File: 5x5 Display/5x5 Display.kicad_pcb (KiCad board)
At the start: 2 copper layers, 129.5 x 129.5 mm, 29 parts, among them J1 TOP, J2 RIGHT, J3 BOTTOM, J4 LEFT

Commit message: buck layout
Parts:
- removed J1: TOP, Magnetic pogo pins:Magnetic Pogo Pin connector 4P
- removed J2: RIGHT, Magnetic pogo pins:Magnetic Pogo Pin connector 4P
- removed J3: BOTTOM, Magnetic pogo pins:Magnetic Pogo Pin connector 4P
- removed J4: LEFT, Magnetic pogo pins:Magnetic Pogo Pin connector 4P
- added C1: 47nF, Capacitor_SMD:C_0603_1608Metric, B.Cu at (19.7, 170.6)
- added C2: 30μF, Capacitor_SMD:C_1206_3216Metric, F.Cu at (236.0, 97.5)
- added C3: 0.1μF, Capacitor_SMD:C_0603_1608Metric, F.Cu at (240.3, 93.7)
- added C4: 30μF, Capacitor_SMD:C_1206_3216Metric, F.Cu at (250.4, 98.7)
- added C5: 30μF, Capacitor_SMD:C_1206_3216Metric, F.Cu at (214.4, 97.5)
- added C6: 0.1μF, Capacitor_SMD:C_0603_1608Metric, F.Cu at (218.8, 93.7)
- added C7: 30μF, Capacitor_SMD:C_1206_3216Metric, F.Cu at (228.9, 98.7)
- added C8: 0.1μF, Capacitor_SMD:C_0603_1608Metric, B.Cu at (28.3, 92.0)
- added C9: 0.33μF, Capacitor_SMD:C_0603_1608Metric, B.Cu at (28.3, 89.0)
- added D1: POWER, LED_SMD:LED_0805_2012Metric, B.Cu at (19.8, 100.2)
- added D10: ≥5V, Diode_SMD:D_SOD-323, F.Cu at (1.67, 0.97)
- added D2: FUSE FAULT, LED_SMD:LED_0805_2012Metric, B.Cu at (19.8, 97.1)
- added D3: 3.3V FAULT, LED_SMD:LED_0805_2012Metric, B.Cu at (19.8, 94.1)
- added D4: 5V FAULT, LED_SMD:LED_0805_2012Metric, B.Cu at (19.8, 91.0)
- added D5: CLOCK, LED_SMD:LED_0805_2012Metric, B.Cu at (19.8, 88.0)
- added D6: ≥33V, Diode_SMD:D_SMA, B.Cu at (10.9, 51.1)
- added D7: ≥33V, Diode_SMD:D_SMA, B.Cu at (10.9, 46.6)
- added D8: ≥33V, Diode_SMD:D_SMA, B.Cu at (10.9, 42.0)
- added D9: ≥33V, Diode_SMD:D_SMA, B.Cu at (10.9, 37.5)
- added FUSE1: TPS1663x (VQFN), Package_DFN_QFN:VQFN-24-1EP_4x4mm_P0.5mm_EP2.5x2.5mm_ThermalVias, B.Cu at (20.6, 175.3)
- added L1: 2.2μH, Inductor_SMD:L_6.3x6.3_H3, F.Cu at (245.4, 97.2)
- added L2: 3.3μH, Inductor_SMD:L_6.3x6.3_H3, F.Cu at (223.8, 97.2)
- added NT1: NT, NetTie:NetTie-2_SMD_Pad0.5mm, F.Cu at (0.75, 0.25)
- added NT1: NT, NetTie:NetTie-2_SMD_Pad0.5mm, F.Cu at (239.6, 98.3)
- added NT2: NT, NetTie:NetTie-2_SMD_Pad0.5mm, F.Cu at (218.1, 98.3)
- added POGO1: Left - Pins, Connector_PinSocket_2.54mm:PinSocket_1x05_P2.54mm_Horizontal, F.Cu at (73.7, 80.0)
- added POGO2: Top - Pins, Connector_PinSocket_2.54mm:PinSocket_1x05_P2.54mm_Horizontal, F.Cu at (141.0, 22.9)
- added POGO3: Right - Socket, Connector_PinSocket_2.54mm:PinSocket_1x05_P2.54mm_Horizontal, F.Cu at (198.1, 90.2)
- added POGO4: Bottom - Socket, Connector_PinSocket_2.54mm:PinSocket_1x05_P2.54mm_Horizontal, F.Cu at (130.8, 147.3)
- added R1: 1.5MΩ, Resistor_SMD:R_0603_1608Metric, B.Cu at (15.5, 177.2)
- added R10: 1kΩ, Resistor_SMD:R_0603_1608Metric, B.Cu at (24.0, 100.4)
- added R11: 1.5kΩ, Resistor_SMD:R_0603_1608Metric, B.Cu at (24.0, 97.9)
- added R12: 1.5kΩ, Resistor_SMD:R_0603_1608Metric, B.Cu at (24.0, 95.4)
- added R13: 1.5kΩ, Resistor_SMD:R_0603_1608Metric, B.Cu at (24.0, 92.9)
- added R14: 1.5kΩ, Resistor_SMD:R_0603_1608Metric, B.Cu at (24.0, 90.4)
- added R2: 430kΩ, Resistor_SMD:R_0603_1608Metric, B.Cu at (15.5, 174.7)
- added R3: 75kΩ, Resistor_SMD:R_0603_1608Metric, B.Cu at (15.5, 172.1)
- added R4: 5.6kΩ, Resistor_SMD:R_0603_1608Metric, B.Cu at (15.5, 169.6)
- added R5: 22kΩ, Resistor_SMD:R_0603_1608Metric, B.Cu at (15.5, 167.1)
- added R6: 45Ω, Resistor_SMD:R_0603_1608Metric, F.Cu at (239.4, 102.2)
- added R7: 10kΩ, Resistor_SMD:R_0603_1608Metric, F.Cu at (239.4, 100.5)
- added R8: 74kΩ, Resistor_SMD:R_0603_1608Metric, F.Cu at (217.8, 102.2)
- added R9: 10kΩ, Resistor_SMD:R_0603_1608Metric, F.Cu at (217.8, 100.5)
- added REG1: TPS56637 3.3v, TPS56637:TPS56637 VQFN-HR (10), F.Cu at (239.4, 97.5)
- added REG2: TPS56637 5V, TPS56637:TPS56637 VQFN-HR (10), F.Cu at (217.8, 97.5)
- added REG3: L78M05ABDT, Package_TO_SOT_SMD:TO-252-2, B.Cu at (32.9, 97.5)
- added TP1: VBUS, TestPoint:TestPoint_Pad_D1.5mm, F.Cu at (212.7, 115.5)
- added TP10: GND, TestPoint:TestPoint_Pad_D1.5mm, F.Cu at (223.4, 115.5)
- added TP11: GND, TestPoint:TestPoint_Pad_D1.5mm, F.Cu at (223.4, 119.0)
- added TP12: GND, TestPoint:TestPoint_Pad_D1.5mm, F.Cu at (223.4, 122.6)
- added TP2: VBUS_P, TestPoint:TestPoint_Pad_D1.5mm, F.Cu at (212.7, 119.0)
- added TP3: CLK_LOW, TestPoint:TestPoint_Pad_D1.5mm, F.Cu at (212.7, 122.6)
- added TP4: CLK, TestPoint:TestPoint_Pad_D1.5mm, F.Cu at (216.3, 115.5)
- added TP5: PGOOD, TestPoint:TestPoint_Pad_D1.5mm, F.Cu at (216.3, 119.0)
- added TP6: +3.3v, TestPoint:TestPoint_Pad_D1.5mm, F.Cu at (216.3, 122.6)
- added TP7: +5v, TestPoint:TestPoint_Pad_D1.5mm, F.Cu at (219.8, 115.5)
- added TP8: LED LDO, TestPoint:TestPoint_Pad_D1.5mm, F.Cu at (219.8, 119.0)
- added TP9: AGND, TestPoint:TestPoint_Pad_D1.5mm, F.Cu at (219.8, 122.6)
- added U3: DRV1, Package_SON:WSON-8-1EP_2x2mm_P0.5mm_EP0.9x1.6mm, B.Cu at (37.1, 46.9)
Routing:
- net CLK: track 719.1 -> 0.00 mm
- net +5V: track 0.00 -> 17.6 mm, vias 0 -> 2
- net +3.3V: track 4.86 -> 20.5 mm, vias 2 -> 0
- net Net-(REG2-FB): track 0.00 -> 3.61 mm
- net Net-(REG1-FB): track 0.00 -> 3.61 mm
- added copper zone on F.Cu, net +3.3V
- added copper zone on F.Cu, net +5V
- added copper zone on F.Cu, net AGND
- added copper zone on F.Cu, net Net-(REG1-BOOT)
- added copper zone on F.Cu, net Net-(REG1-SW)
- added copper zone on F.Cu, net Net-(REG2-BOOT)
- added copper zone on F.Cu, net Net-(REG2-SW)
- added copper zone on F.Cu, net VBUS_P
- removed copper zone on B.Cu, net +3.3V
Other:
- board size 129.5 x 129.5 mm -> 182.4 x 129.5 mm
- copper layers 2 -> 4
- board text removed: "3.3V"
- board text removed: "CLK"
- board text removed: "GND"
- board text removed: "PROTOTYPE"
- board text removed: "Pips801 2026"
- board text removed: "Stackable 5x5 Minibadge display"

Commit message: Initial route complete
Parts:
- removed D10: ≥5V, Diode_SMD:D_SOD-323
- removed the NT1 at (0.75, 0.25)
- removed TP10, TP11: GND, TestPoint:TestPoint_Pad_D1.5mm
- removed TP2: VBUS_P, TestPoint:TestPoint_Pad_D1.5mm
- removed TP4: CLK, TestPoint:TestPoint_Pad_D1.5mm
- removed TP5: PGOOD, TestPoint:TestPoint_Pad_D1.5mm
- removed TP9: AGND, TestPoint:TestPoint_Pad_D1.5mm
- added kibuzzard-69632EEE: G***, kibuzzard-69632EEE, B.Cu at (139.1, 107.3)
- added kibuzzard-69632F12: G***, kibuzzard-69632F12, B.Cu at (136.1, 110.5)
- added kibuzzard-69632F20: G***, kibuzzard-69632F20, B.Cu at (136.1, 113.7)
- added kibuzzard-69632F6C: G***, kibuzzard-69632F6C, B.Cu at (137.3, 116.8)
- added kibuzzard-69632F9B: G***, kibuzzard-69632F9B, B.Cu at (139.2, 104.1)
- added kibuzzard-69633F6A: G***, kibuzzard-69633F6A, B.Cu at (117.2, 107.3)
- added kibuzzard-6963405F: G***, kibuzzard-6963405F, B.Cu at (117.2, 110.5)
- added kibuzzard-696340B6: G***, kibuzzard-696340B6, B.Cu at (117.2, 113.7)
- added kibuzzard-69634119: G***, kibuzzard-69634119, B.Cu at (117.2, 104.1)
- added kibuzzard-6963413C: G***, kibuzzard-6963413C, B.Cu at (117.2, 116.8)
- C2, C3, C4, C5, C6, C7, L1, L2, NT1, NT2, R6, R7, R8, R9, REG1, REG2, TP1, TP12, TP3, TP6, TP7, TP8: moved to B.Cu
- MB13, MB14, MB15: footprint MiniBadge:MiniBadge_Slot_Reflective -> MiniBadge:MiniBadge_Slot_Basic
- moved D7 187.7 mm to (194.3, 86.4), turned to 90 degrees
- moved R1 155.7 mm to (136.5, 79.2), turned to 90 degrees
- moved R2 155.4 mm to (138.1, 79.2), turned to 90 degrees
- moved R3 155.1 mm to (139.7, 79.2), turned to 90 degrees
- moved D6 152.9 mm to (134.6, 141.0)
- moved R4 152.0 mm to (140.5, 83.2)
- moved C1 150.0 mm to (140.5, 81.6)
- moved R5 149.7 mm to (140.5, 84.8)
- moved FUSE1 147.5 mm to (136.1, 83.6), turned to -90 degrees
- moved C9 145.1 mm to (173.4, 87.6), turned to 90 degrees
- moved REG3 136.6 mm to (168.9, 84.8), turned to 90 degrees
- moved C8 136.3 mm to (164.5, 87.6), turned to 90 degrees
- moved U3 130.9 mm to (163.6, 80.7), turned to -90 degrees
- moved D4 126.4 mm to (143.5, 116.8)
- moved R13 125.9 mm to (147.6, 116.8)
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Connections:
- FUSE1 pad 25: (no net) -> GND
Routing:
- net CLK: track 0.00 -> 668.6 mm, vias 0 -> 2
- net CLK_LOW: track 0.00 -> 310.7 mm, vias 0 -> 2
- net +5V LED: track 0.00 -> 75.5 mm
- net PG_3V: track 0.00 -> 66.2 mm, vias 0 -> 2
- net FAULT: track 0.00 -> 51.4 mm, vias 0 -> 2
- net PG_5V: track 0.00 -> 46.8 mm, vias 0 -> 2
- net PGOOD: track 0.00 -> 24.8 mm, vias 0 -> 3
- net +3.3V: track 20.5 -> 0.75 mm, vias 0 -> 9
- net GND: track 0.00 -> 18.3 mm, vias 0 -> 40
- net Net-(FUSE1-OVP): track 0.00 -> 5.13 mm
- net VBUS: track 0.00 -> 4.15 mm, vias 0 -> 6
- net Net-(FUSE1-UVLO): track 0.00 -> 4.07 mm
- net Net-(FUSE1-dVdT): track 0.00 -> 2.65 mm
- net IMON: track 0.00 -> 2.55 mm
- net Net-(D5-A): track 0.00 -> 2.38 mm
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- added copper zone on B.Cu, net +3.3V
- added copper zone on In2.Cu, net +3.3V
- added copper zone on B.Cu, net +5V
- added copper zone on B.Cu, net AGND
- added copper zone on B.Cu, net CLK
- added copper zone on B.Cu, net GND
- added copper zone on In1.Cu, net GND
- added copper zone on B.Cu, net Net-(REG1-BOOT)
- added copper zone on B.Cu, net Net-(REG1-SW)
- added copper zone on B.Cu, net Net-(REG2-BOOT)
- added copper zone on B.Cu, net Net-(REG2-SW)
- added copper zone on B.Cu, net VBUS
- added copper zone on F.Cu, net VBUS
- added copper zone on B.Cu, net VBUS_P
- removed copper zone on F.Cu, net +3.3V
- removed copper zone on F.Cu, net +5V
- removed copper zone on F.Cu, net AGND
- removed copper zone on F.Cu, net GND
- removed copper zone on F.Cu, net Net-(REG1-BOOT)
- removed copper zone on F.Cu, net Net-(REG1-SW)
- removed copper zone on F.Cu, net Net-(REG2-BOOT)
- removed copper zone on F.Cu, net Net-(REG2-SW)
- removed copper zone on F.Cu, net VBUS_P
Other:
- board size 182.4 x 129.5 mm -> 129.5 x 129.5 mm
- board text added: "Stackup F = VBUS In1 = GND In2 = 3.3V B = 5V, CLK, signals"

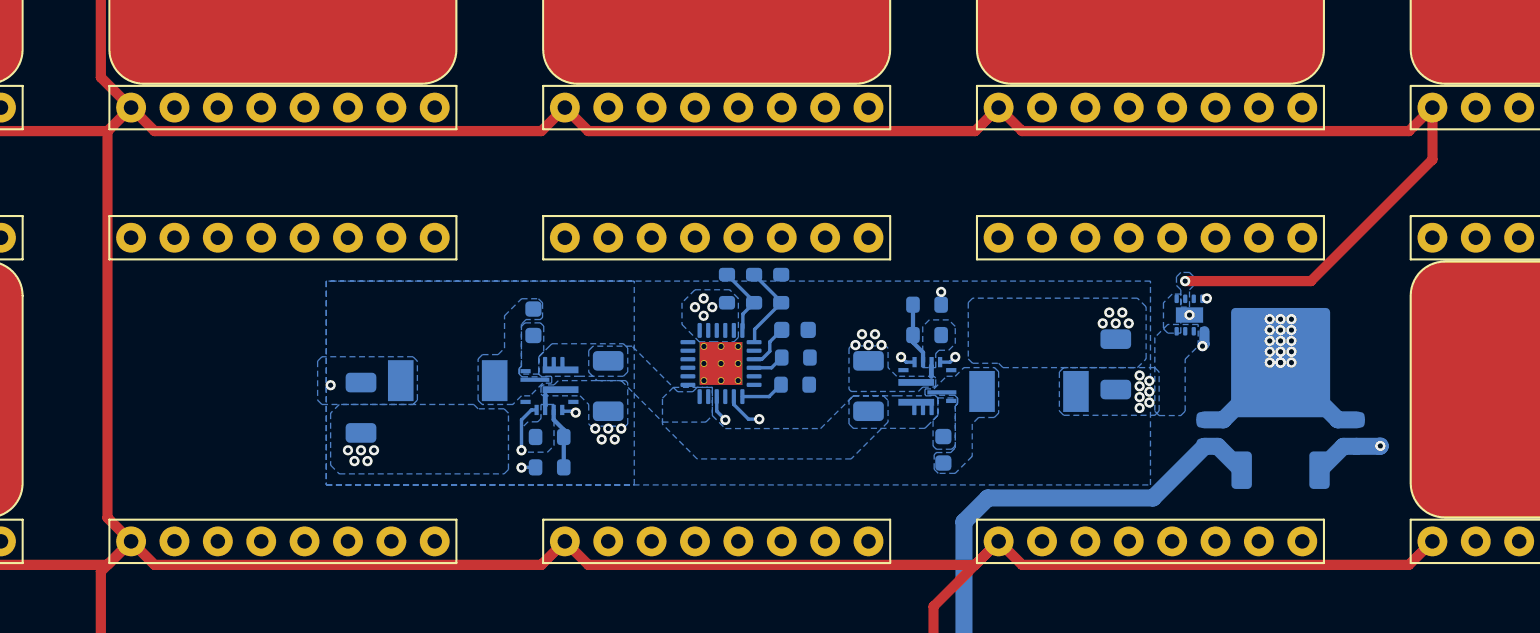
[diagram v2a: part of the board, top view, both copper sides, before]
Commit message: Fix CLK_LOW routing
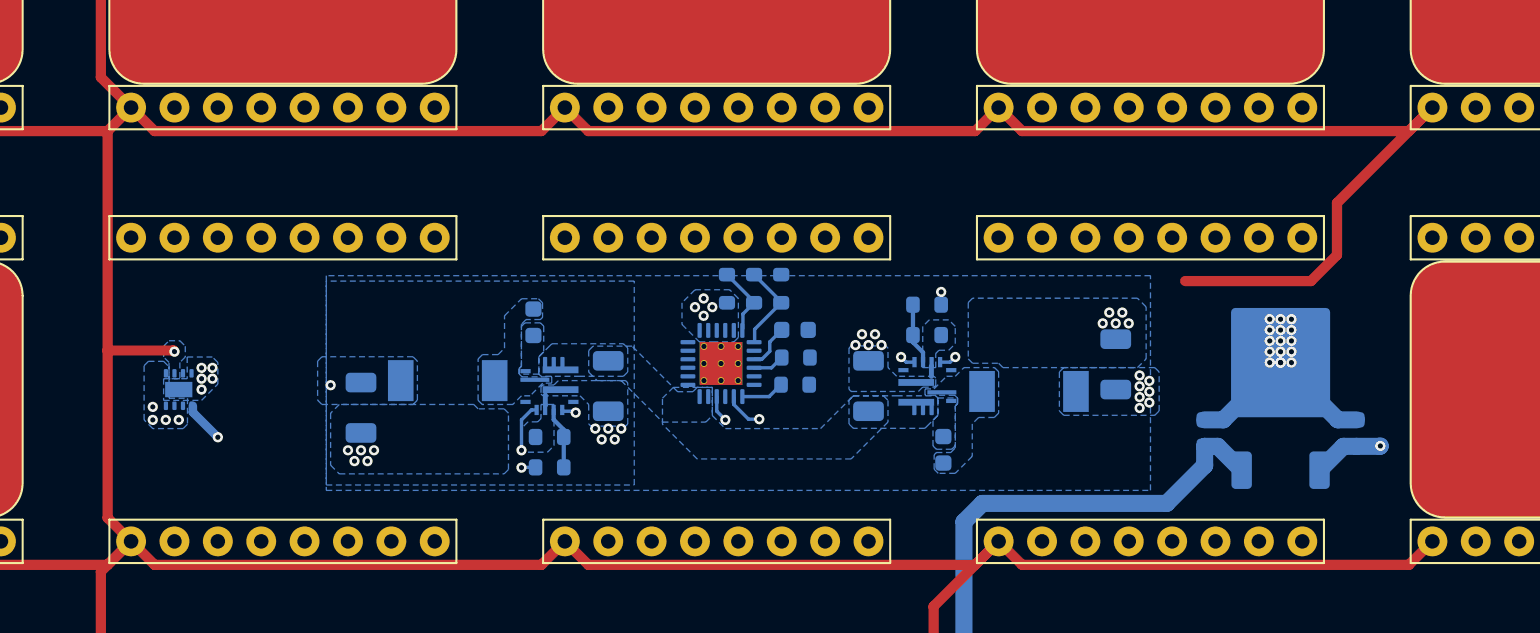
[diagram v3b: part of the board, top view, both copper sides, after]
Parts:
- moved U3 59.3 mm to (104.4, 85.1)
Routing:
- net CLK_LOW: track 310.7 -> 571.4 mm
- net CLK: track 668.6 -> 672.5 mm
- net +5V LED: track 75.5 -> 76.2 mm
- net PGOOD: track 24.8 -> 24.2 mm
- net GND: vias 40 -> 43
- net +3.3V: vias 9 -> 13

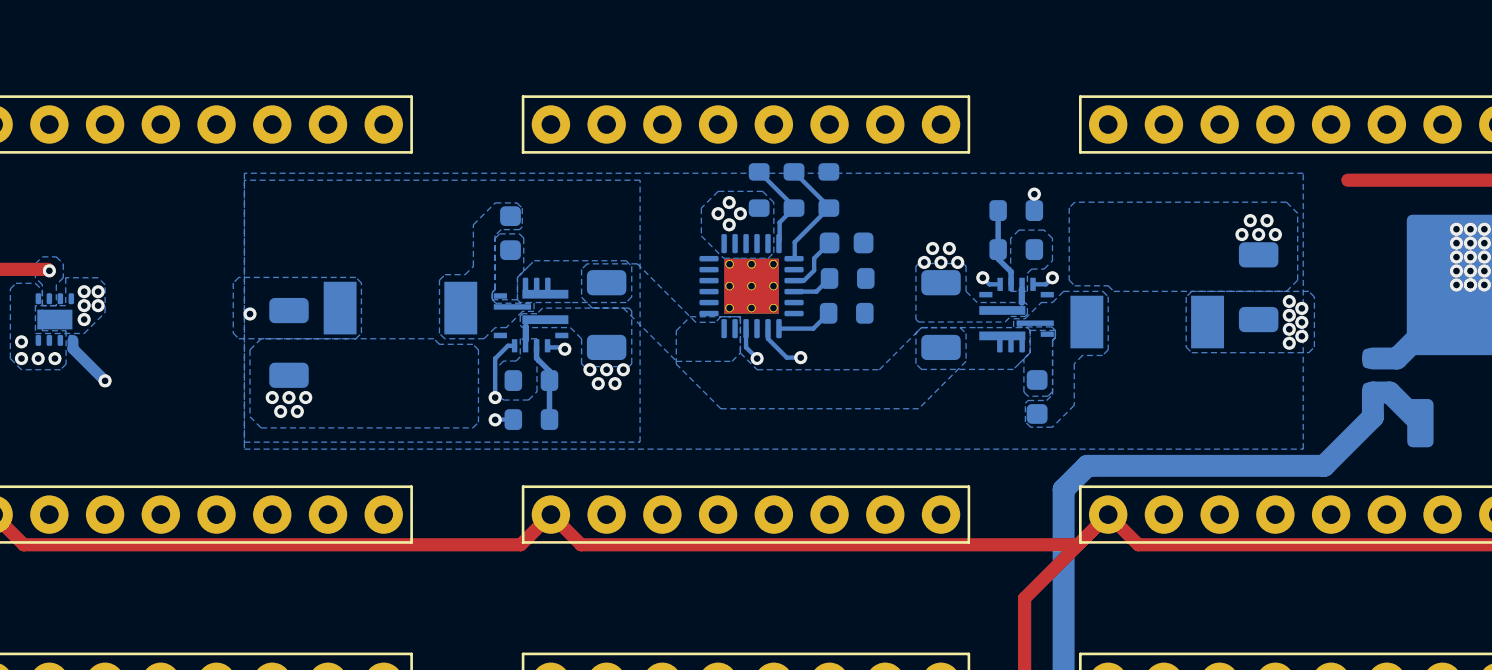
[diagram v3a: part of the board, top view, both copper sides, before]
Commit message: Add silkscreen text, rectangle, and tented vias
Added a large silkscreen label '5X5 DISPLAY PROTOTYPE' and a rectangle to the PCB. Adjusted the positions of several component references. Enabled tenting on multiple vias for nets 2, 4, and 9. Updated the PDF output to reflect these changes.
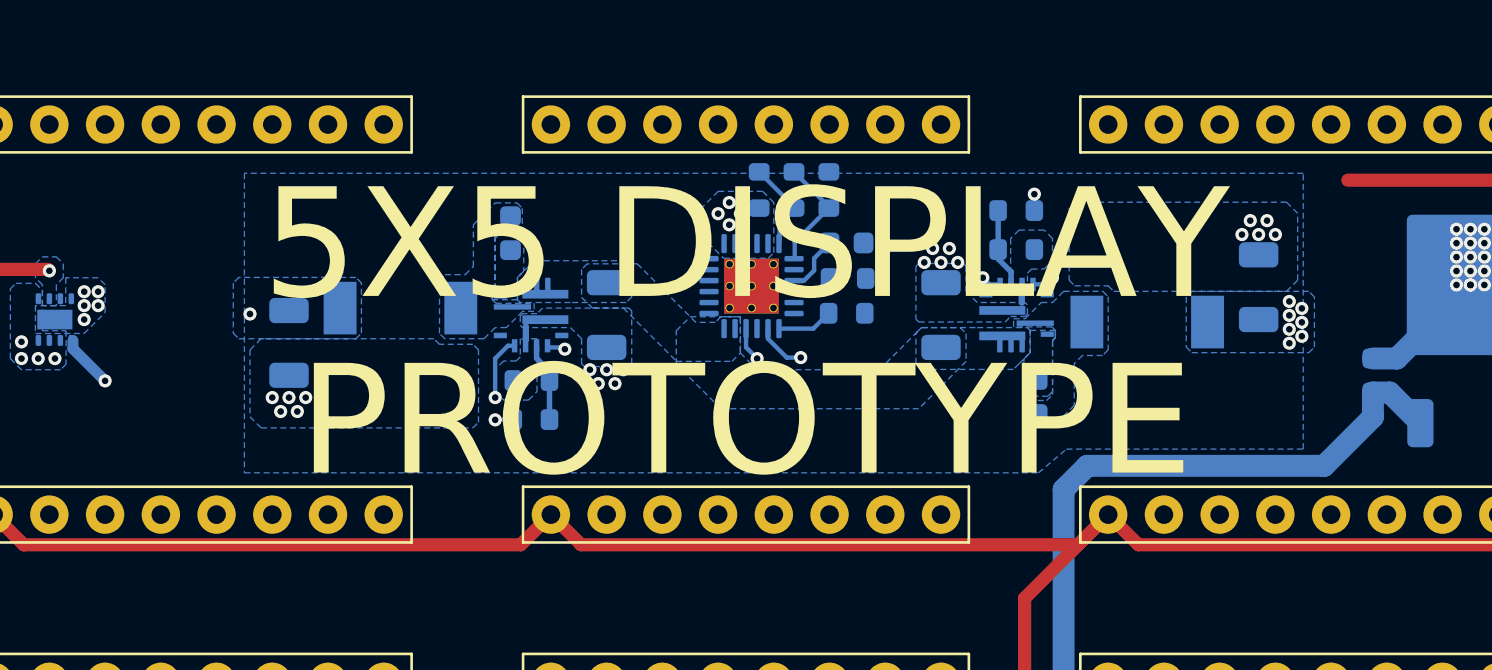
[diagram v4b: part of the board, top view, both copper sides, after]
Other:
- board text added: "5X5 DISPLAY PROTOTYPE"
